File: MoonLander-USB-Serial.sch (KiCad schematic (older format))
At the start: 8 parts

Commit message: first whack at layout - unrouted
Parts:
- removed L?: CHOKE, symbol CHOKE
- C301, C302, C303, C304: renamed from C?; footprint (none) -> Capacitors_SMD:C_0402
- IC301: renamed from IC?; footprint (none) -> GrayCatLabs:SOT143B
- IC302: renamed from IC?; footprint (none) -> Housings_DFN_QFN:QFN-24-1EP_4x4mm_Pitch0.5mm
- R301: renamed from R?; footprint (none) -> Resistors_SMD:R_0402
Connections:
- net GND: now also IC302.2 (GND)
- net USB_D+: now also IC301.3 (I/O_2), IC302.3 (D+)
- net USB_D-: now also IC301.2 (I/O_1), IC302.4 (D-)
- net at IC302.16 (VPP): now also C303.1
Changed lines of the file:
@@
 Comment4 ""
 $EndDescr
-$Comp
-L CHOKE L?
-U 1 1 565F92DE
-P 3250 4050
-F 0 "L?" H 3250 4200 60  0000 C CNN
-F 1 "CHOKE" H 3250 3850 60  0000 C CNN
-F 2 "" H 3300 4000 60  0000 C CNN
-F 3 "" H 3300 4000 60  0000 C CNN
-	1    3250 4050
-	1    0    0    -1
-$EndComp
 Text HLabel 2600 4000 0    60   BiDi ~ 0
 USB_D+
@@
 USB_D-
 Wire Wire Line
-	2600 4000 3050 4000
-Wire Wire Line
-	3050 4150 2600 4150
-$Comp
-L PRTR5V0U2X IC?
+	2600 4000 6200 4000
+Wire Wire Line
+	2600 4150 4650 4150
+$Comp
+L PRTR5V0U2X IC301
 U 1 1 565F944D
 P 3850 3250
-F 0 "IC?" H 3650 3450 60  0000 C CNN
+F 0 "IC301" H 3650 3450 60  0000 C CNN
 F 1 "PRTR5V0U2X" H 3850 3050 60  0000 C CNN
-F 2 "" H 3850 3250 60  0000 C CNN
+F 2 "GrayCatLabs:SOT143B" H 3850 3250 60  0001 C CNN
 F 3 "" H 3850 3250 60  0000 C CNN
 	1    3850 3250
@@
 $EndComp
 $Comp
-L 5V_USB #PWR?
+L 5V_USB #PWR012
 U 1 1 565F94A8
 P 3100 3050
-F 0 "#PWR?" H 3100 2900 50  0001 C CNN
+F 0 "#PWR012" H 3100 2900 50  0001 C CNN
 F 1 "5V_USB" H 3100 3190 50  0000 C CNN
 F 2 "" H 3100 3050 60  0000 C CNN
@@
 $EndComp
 $Comp
-L GND #PWR?
+L GND #PWR013
 U 1 1 565F94C0
 P 3100 3400
-F 0 "#PWR?" H 3100 3150 50  0001 C CNN
+F 0 "#PWR013" H 3100 3150 50  0001 C CNN
 F 1 "GND" H 3100 3250 50  0000 C CNN
 F 2 "" H 3100 3400 50  0000 C CNN
@@
 	3100 3200 3100 3050
 Wire Wire Line
-	3450 4000 6200 4000
-Wire Wire Line
 	4500 4000 4500 3300
 Wire Wire Line
 	4500 3300 4350 3300
 Wire Wire Line
-	4650 3200 4650 4150
+	4650 4150 4650 3200
 Wire Wire Line
 	4650 3200 4350 3200
@@
 Connection ~ 4650 4100
 $Comp
-L CP2110-GM IC?
+L CP2110-GM IC302
 U 1 1 565FB418
 P 6900 3950
-F 0 "IC?" H 6500 4900 60  0000 C CNN
+F 0 "IC302" H 6500 4900 60  0000 C CNN
 F 1 "CP2110-GM" H 7100 3050 60  0000 C CNN
-F 2 "" H 6900 3950 60  0000 C CNN
+F 2 "Housings_DFN_QFN:QFN-24-1EP_4x4mm_Pitch0.5mm" H 6900 3950 60  0001 C CNN
 F 3 "" H 6900 3950 60  0000 C CNN
 	1    6900 3950
@@
 Wire Wire Line
 	4650 4100 6200 4100
-Wire Wire Line
-	4650 4150 3450 4150
-$Comp
-L 5V_USB #PWR?
+$Comp
+L 5V_USB #PWR014
 U 1 1 565FB66D
 P 5000 3550
-F 0 "#PWR?" H 5000 3400 50  0001 C CNN
+F 0 "#PWR014" H 5000 3400 50  0001 C CNN
 F 1 "5V_USB" H 5000 3690 50  0000 C CNN
 F 2 "" H 5000 3550 60  0000 C CNN
@@
 	5000 3900 6200 3900
 $Comp
-L C C?
+L C C301
 U 1 1 565FB6AC
 P 5000 4600
-F 0 "C?" H 5025 4700 50  0000 L CNN
+F 0 "C301" H 5025 4700 50  0000 L CNN
 F 1 "1uF" H 5025 4500 50  0000 L CNN
-F 2 "" H 5038 4450 50  0000 C CNN
+F 2 "Capacitors_SMD:C_0402" H 5038 4450 50  0001 C CNN
 F 3 "" H 5000 4600 50  0000 C CNN
 	1    5000 4600
@@
 Connection ~ 5000 3900
 $Comp
-L C C?
+L C C303
 U 1 1 565FB734
 P 5450 4600
-F 0 "C?" H 5475 4700 50  0000 L CNN
+F 0 "C303" H 5475 4700 50  0000 L CNN
 F 1 "4.7uF" H 5475 4500 50  0000 L CNN
-F 2 "" H 5488 4450 50  0000 C CNN
+F 2 "Capacitors_SMD:C_0402" H 5488 4450 50  0001 C CNN
 F 3 "" H 5450 4600 50  0000 C CNN
 	1    5450 4600
@@
 $EndComp
 Wire Wire Line
-	6200 4350 5450 4350
-Wire Wire Line
-	5450 4350 5450 4450
+	6200 4300 5450 4300
+Wire Wire Line
+	5450 4300 5450 4450
 Wire Wire Line
 	6200 4600 5950 4600
 Wire Wire Line
-	5950 4600 5950 4850
-Wire Wire Line
-	5950 4850 5000 4850
+	5950 4850 5950 4500
+Wire Wire Line
+	5000 4850 5950 4850
 Wire Wire Line
 	5000 4750 5000 4950
@@
 Connection ~ 5450 4850
 $Comp
-L C C?
+L C C304
 U 1 1 565FB9DD
 P 5900 3400
-F 0 "C?" H 5925 3500 50  0000 L CNN
+F 0 "C304" H 5925 3500 50  0000 L CNN
 F 1 "1uF" H 5925 3300 50  0000 L CNN
-F 2 "" H 5938 3250 50  0000 C CNN
+F 2 "Capacitors_SMD:C_0402" H 5938 3250 50  0001 C CNN
 F 3 "" H 5900 3400 50  0000 C CNN
 	1    5900 3400
@@
 	6050 3400 6200 3400
 $Comp
-L GND #PWR?
+L GND #PWR015
 U 1 1 565FBA98
 P 5000 4950
-F 0 "#PWR?" H 5000 4700 50  0001 C CNN
+F 0 "#PWR015" H 5000 4700 50  0001 C CNN
 F 1 "GND" H 5000 4800 50  0000 C CNN
 F 2 "" H 5000 4950 50  0000 C CNN
@@
 $EndComp
 $Comp
-L GND #PWR?
+L GND #PWR016
 U 1 1 565FBABC
 P 5400 3450
-F 0 "#PWR?" H 5400 3200 50  0001 C CNN
+F 0 "#PWR016" H 5400 3200 50  0001 C CNN
 F 1 "GND" H 5400 3300 50  0000 C CNN
 F 2 "" H 5400 3450 50  0000 C CNN
@@
 	5950 3150 5950 2900
 $Comp
-L VCC #PWR?
+L VCC #PWR017
 U 1 1 565FBB9F
 P 5400 2800
-F 0 "#PWR?" H 5400 2650 50  0001 C CNN
+F 0 "#PWR017" H 5400 2650 50  0001 C CNN
 F 1 "VCC" H 5400 2950 50  0000 C CNN
 F 2 "" H 5400 2800 50  0000 C CNN
@@
 $EndComp
 $Comp
-L C C?
+L C C302
 U 1 1 565FBBC3
 P 5400 3150
-F 0 "C?" H 5425 3250 50  0000 L CNN
+F 0 "C302" H 5425 3250 50  0000 L CNN
 F 1 "0.1uF" H 5425 3050 50  0000 L CNN
-F 2 "" H 5438 3000 50  0000 C CNN
+F 2 "Capacitors_SMD:C_0402" H 5438 3000 50  0001 C CNN
 F 3 "" H 5400 3150 50  0000 C CNN
 	1    5400 3150
@@
 Connection ~ 5000 4850
 $Comp
-L R R?
+L R R301
 U 1 1 565FC58B
 P 7800 2900
-F 0 "R?" V 7880 2900 50  0000 C CNN
+F 0 "R301" V 7880 2900 50  0000 C CNN
 F 1 "10k" V 7800 2900 50  0000 C CNN
-F 2 "" V 7730 2900 50  0000 C CNN
+F 2 "Resistors_SMD:R_0402" V 7730 2900 50  0001 C CNN
 F 3 "" H 7800 2900 50  0000 C CNN
 	1    7800 2900
@@
 	7800 3150 7800 3050
 $Comp
-L VCC #PWR?
+L VCC #PWR018
 U 1 1 565FC608
 P 7800 2650
-F 0 "#PWR?" H 7800 2500 50  0001 C CNN
+F 0 "#PWR018" H 7800 2500 50  0001 C CNN
 F 1 "VCC" H 7800 2800 50  0000 C CNN
 F 2 "" H 7800 2650 50  0000 C CNN
@@
 Text HLabel 8300 3650 2    60   Input ~ 0
 ISP_TXD
+Wire Wire Line
+	5950 4500 6200 4500
+Connection ~ 5950 4600
 $EndSCHEMATC

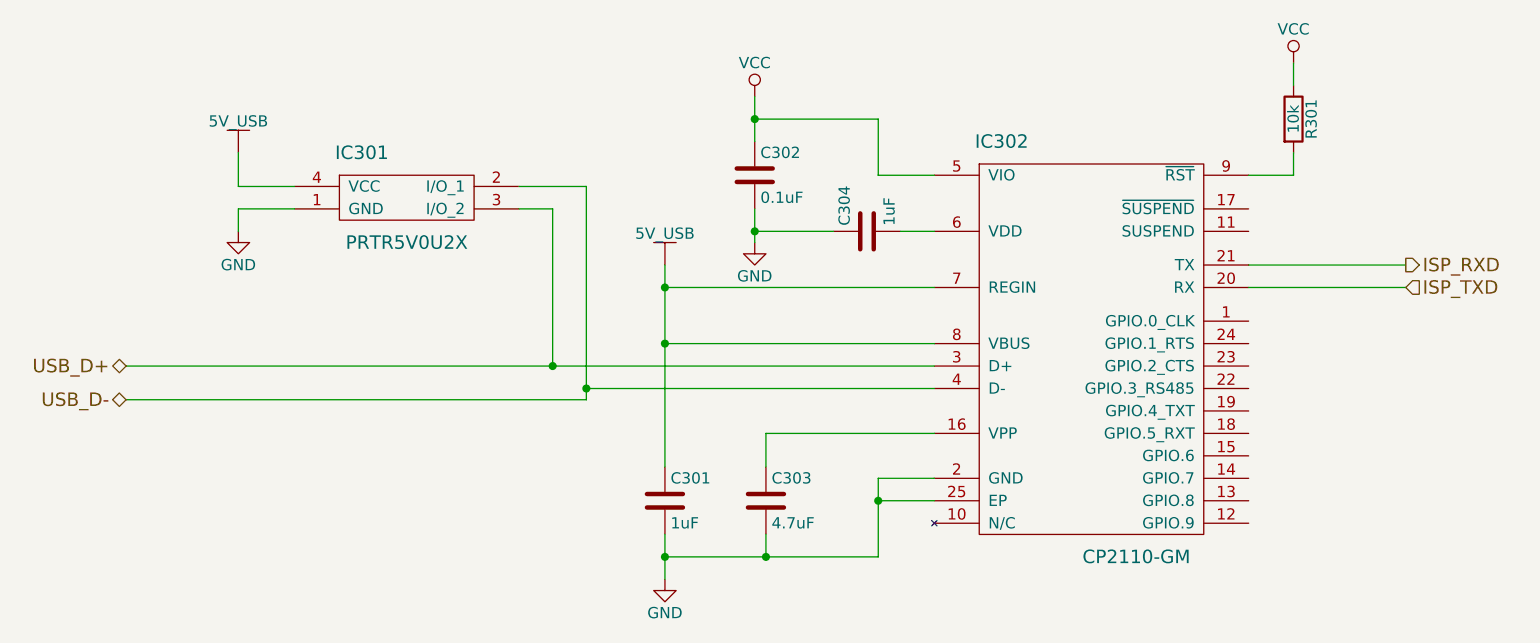
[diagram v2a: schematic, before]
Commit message: simplified 2 layer version
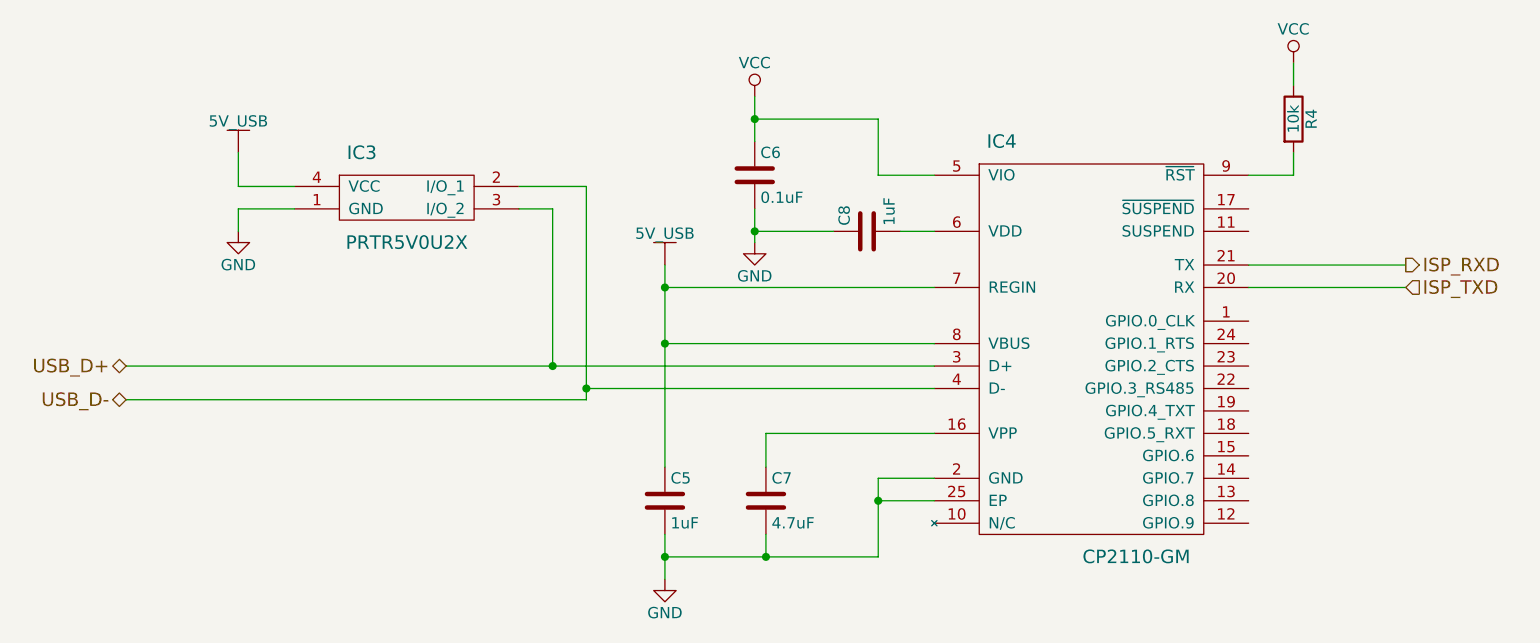
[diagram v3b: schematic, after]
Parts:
- renumbered C301 to C5, C302 to C6, C303 to C7, C304 to C8, IC301 to IC3, IC302 to IC4, R301 to R4
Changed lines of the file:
@@
 $Descr A4 11693 8268
 encoding utf-8
-Sheet 3 6
+Sheet 3 5
 Title ""
 Date ""
@@
 	2600 4150 4650 4150
 $Comp
-L PRTR5V0U2X IC301
+L PRTR5V0U2X IC3
 U 1 1 565F944D
 P 3850 3250
-F 0 "IC301" H 3650 3450 60  0000 C CNN
+F 0 "IC3" H 3650 3450 60  0000 C CNN
 F 1 "PRTR5V0U2X" H 3850 3050 60  0000 C CNN
 F 2 "GrayCatLabs:SOT143B" H 3850 3250 60  0001 C CNN
@@
 $EndComp
 $Comp
-L 5V_USB #PWR012
+L 5V_USB #PWR010
 U 1 1 565F94A8
 P 3100 3050
-F 0 "#PWR012" H 3100 2900 50  0001 C CNN
+F 0 "#PWR010" H 3100 2900 50  0001 C CNN
 F 1 "5V_USB" H 3100 3190 50  0000 C CNN
 F 2 "" H 3100 3050 60  0000 C CNN
@@
 $EndComp
 $Comp
-L GND #PWR013
+L GND #PWR011
 U 1 1 565F94C0
 P 3100 3400
-F 0 "#PWR013" H 3100 3150 50  0001 C CNN
+F 0 "#PWR011" H 3100 3150 50  0001 C CNN
 F 1 "GND" H 3100 3250 50  0000 C CNN
 F 2 "" H 3100 3400 50  0000 C CNN
@@
 Connection ~ 4650 4100
 $Comp
-L CP2110-GM IC302
+L CP2110-GM IC4
 U 1 1 565FB418
 P 6900 3950
-F 0 "IC302" H 6500 4900 60  0000 C CNN
+F 0 "IC4" H 6500 4900 60  0000 C CNN
 F 1 "CP2110-GM" H 7100 3050 60  0000 C CNN
 F 2 "Housings_DFN_QFN:QFN-24-1EP_4x4mm_Pitch0.5mm" H 6900 3950 60  0001 C CNN
@@
 	4650 4100 6200 4100
 $Comp
-L 5V_USB #PWR014
+L 5V_USB #PWR012
 U 1 1 565FB66D
 P 5000 3550
-F 0 "#PWR014" H 5000 3400 50  0001 C CNN
+F 0 "#PWR012" H 5000 3400 50  0001 C CNN
 F 1 "5V_USB" H 5000 3690 50  0000 C CNN
 F 2 "" H 5000 3550 60  0000 C CNN
@@
 	5000 3900 6200 3900
 $Comp
-L C C301
+L C C5
 U 1 1 565FB6AC
 P 5000 4600
-F 0 "C301" H 5025 4700 50  0000 L CNN
+F 0 "C5" H 5025 4700 50  0000 L CNN
 F 1 "1uF" H 5025 4500 50  0000 L CNN
 F 2 "Capacitors_SMD:C_0402" H 5038 4450 50  0001 C CNN
@@
 Connection ~ 5000 3900
 $Comp
-L C C303
+L C C7
 U 1 1 565FB734
 P 5450 4600
-F 0 "C303" H 5475 4700 50  0000 L CNN
+F 0 "C7" H 5475 4700 50  0000 L CNN
 F 1 "4.7uF" H 5475 4500 50  0000 L CNN
 F 2 "Capacitors_SMD:C_0402" H 5488 4450 50  0001 C CNN
@@
 Connection ~ 5450 4850
 $Comp
-L C C304
+L C C8
 U 1 1 565FB9DD
 P 5900 3400
-F 0 "C304" H 5925 3500 50  0000 L CNN
+F 0 "C8" H 5925 3500 50  0000 L CNN
 F 1 "1uF" H 5925 3300 50  0000 L CNN
 F 2 "Capacitors_SMD:C_0402" H 5938 3250 50  0001 C CNN
@@
 	6050 3400 6200 3400
 $Comp
-L GND #PWR015
+L GND #PWR013
 U 1 1 565FBA98
 P 5000 4950
-F 0 "#PWR015" H 5000 4700 50  0001 C CNN
+F 0 "#PWR013" H 5000 4700 50  0001 C CNN
 F 1 "GND" H 5000 4800 50  0000 C CNN
 F 2 "" H 5000 4950 50  0000 C CNN
@@
 $EndComp
 $Comp
-L GND #PWR016
+L GND #PWR014
 U 1 1 565FBABC
 P 5400 3450
-F 0 "#PWR016" H 5400 3200 50  0001 C CNN
+F 0 "#PWR014" H 5400 3200 50  0001 C CNN
 F 1 "GND" H 5400 3300 50  0000 C CNN
 F 2 "" H 5400 3450 50  0000 C CNN
@@
 	5950 3150 5950 2900
 $Comp
-L VCC #PWR017
+L VCC #PWR015
 U 1 1 565FBB9F
 P 5400 2800
-F 0 "#PWR017" H 5400 2650 50  0001 C CNN
+F 0 "#PWR015" H 5400 2650 50  0001 C CNN
 F 1 "VCC" H 5400 2950 50  0000 C CNN
 F 2 "" H 5400 2800 50  0000 C CNN
@@
 $EndComp
 $Comp
-L C C302
+L C C6
 U 1 1 565FBBC3
 P 5400 3150
-F 0 "C302" H 5425 3250 50  0000 L CNN
+F 0 "C6" H 5425 3250 50  0000 L CNN
 F 1 "0.1uF" H 5425 3050 50  0000 L CNN
 F 2 "Capacitors_SMD:C_0402" H 5438 3000 50  0001 C CNN
@@
 Connection ~ 5000 4850
 $Comp
-L R R301
+L R R4
 U 1 1 565FC58B
 P 7800 2900
-F 0 "R301" V 7880 2900 50  0000 C CNN
+F 0 "R4" V 7880 2900 50  0000 C CNN
 F 1 "10k" V 7800 2900 50  0000 C CNN
 F 2 "Resistors_SMD:R_0402" V 7730 2900 50  0001 C CNN
@@
 	7800 3150 7800 3050
 $Comp
-L VCC #PWR018
+L VCC #PWR016
 U 1 1 565FC608
 P 7800 2650
-F 0 "#PWR018" H 7800 2500 50  0001 C CNN
+F 0 "#PWR016" H 7800 2500 50  0001 C CNN
 F 1 "VCC" H 7800 2800 50  0000 C CNN
 F 2 "" H 7800 2650 50  0000 C CNN
